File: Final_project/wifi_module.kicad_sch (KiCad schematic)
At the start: 3 parts, among them U4 ESP32-WROOM-32

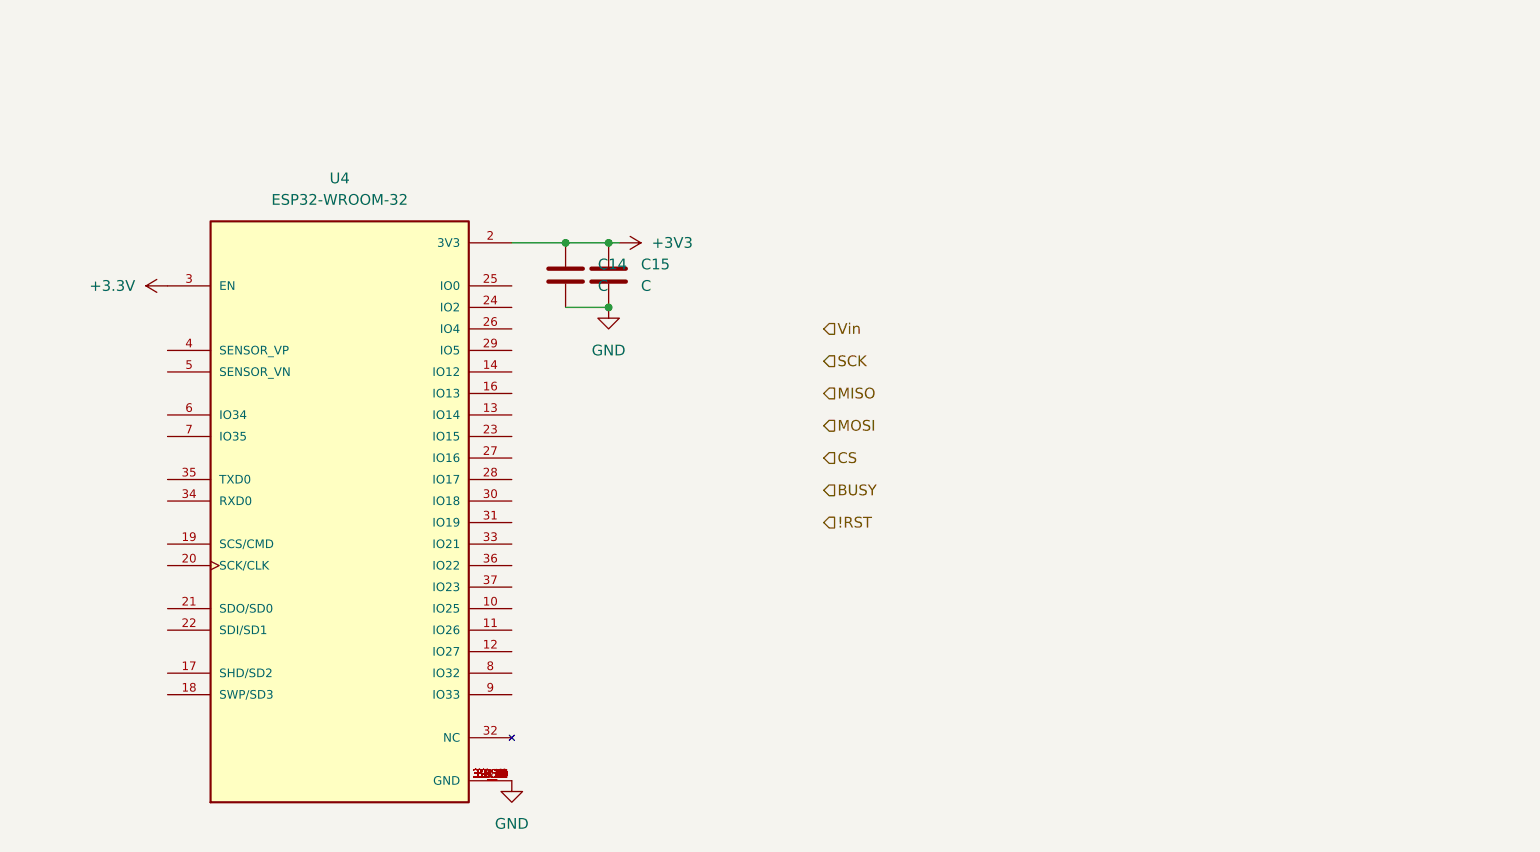
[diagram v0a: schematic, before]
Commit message: Complete wifi module airlift
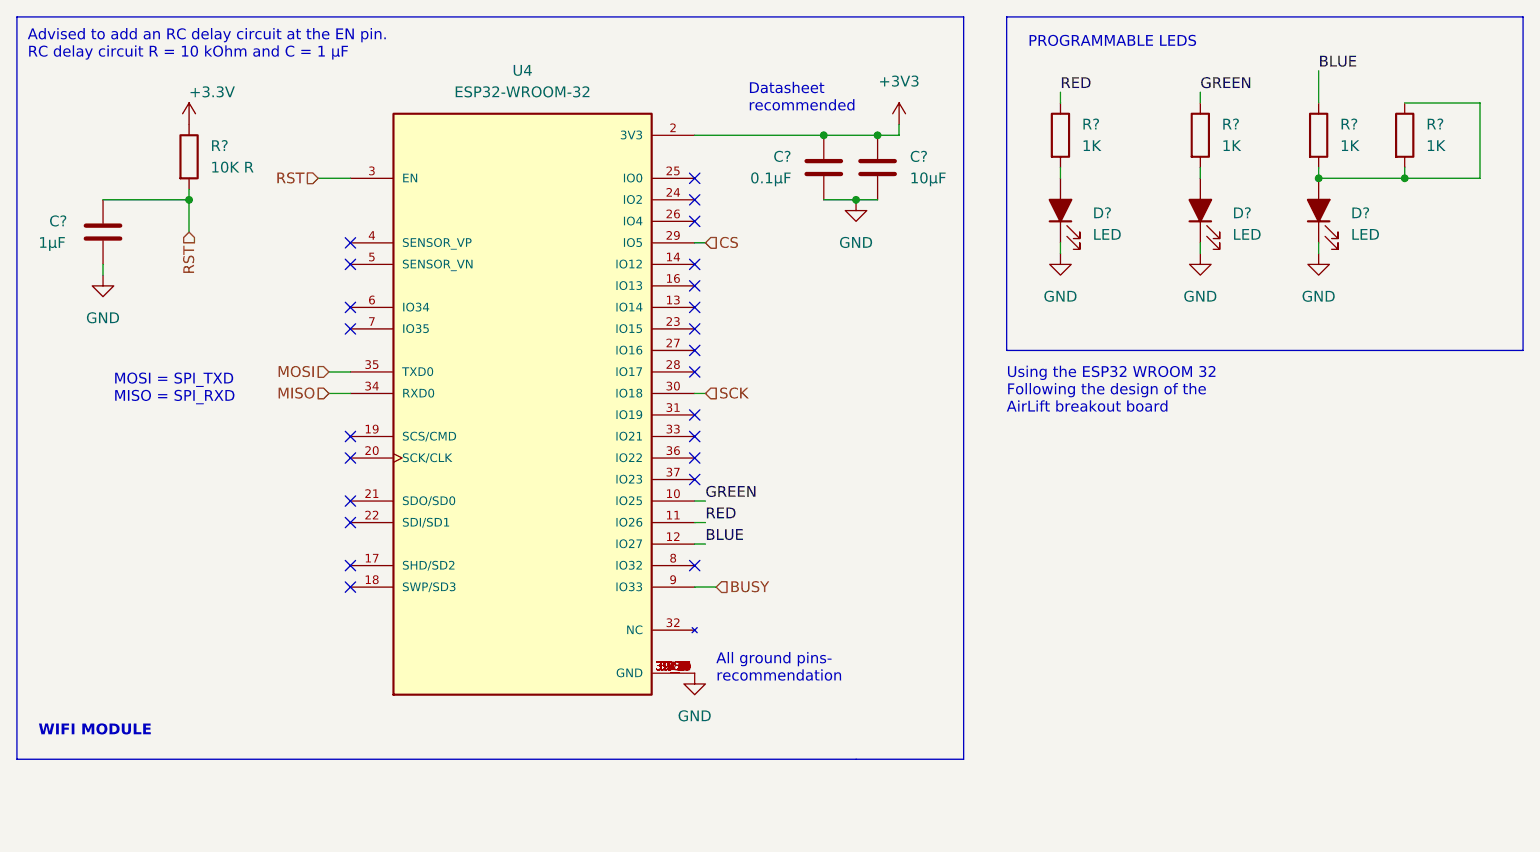
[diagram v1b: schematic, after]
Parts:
- removed C14, C15: C, Capacitor_SMD:C_0603_1608Metric, symbol Device:C
- added C?: 10µF, Final_project:GRM188R61E106KA73D, symbol Device:C
- added C?: 0.1µF, Final_project:CL10B104JB8NNNC, symbol Device:C
- added C?: 1µF, Final_project:CL10B105KA8NNNC, symbol Device:C
- added D? (x3): LED, Final_project:LTST-C170TBKT, symbol Device:LED_Filled
- added R? (x4): 1K, Final_project:RC0603FR-071KL, symbol Device:R
- added R?: 10K R, Resistor_SMD:R_0805_2012Metric, symbol Device:R
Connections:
- net +3.3V: now also R?.1; no longer U4.3 (EN)
- net +3V3: now also C?.1, C?.1
- net BUSY: now also U4.9 (IO33)
- net CS: now also U4.29 (IO5)
- net GND: now also C?.1, C?.2, C?.2, D?.1 (K), D?.1 (K), D?.1 (K)
- net MISO: now also U4.34 (RXD0)
- net MOSI: now also U4.35 (TXD0)
- net SCK: now also U4.30 (IO18)
- net GREEN: now reaches U4.10 (IO25)
- net GREEN: now also R?.1
- net RED: now reaches U4.11 (IO26)
- net RED: now also R?.1
- net BLUE: now reaches U4.12 (IO27)
- net BLUE: now also R?.1
- new net: D?.2 (A), R?.1, R?.2, R?.2
- new net: D?.2 (A), R?.2 (x2)
- new net RST: C?.2, R?.2, U4.3 (EN)
- no-connect marks 0 -> 24
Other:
- note added: "Advised to add an RC delay circuit at the EN pin. RC delay circuit R = 10 kOhm and C = 1 μF"
- note added: "All ground pins- recommendation"
- note added: "Datasheet recommended"
- note added: "MOSI = SPI_TXD MISO = SPI_RXD"
- note added: "PROGRAMMABLE LEDS"
- note added: "Using the ESP32 WROOM 32 Following the design of the AirLift breakout board"
- note added: "WIFI MODULE"
- moved on the sheet: U4

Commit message: Add light sensing sheet
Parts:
- gave numbers to parts that had none: 11
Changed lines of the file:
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@@
   (symbol (lib_id "power:+3.3V") (at 35.56 26.67 0) (unit 1)
     (in_bom yes) (on_board yes)
-    (property "Reference" "#PWR?" (id 0) (at 35.56 30.48 0)
+    (property "Reference" "#PWR0136" (id 0) (at 35.56 30.48 0)
       (effects (font (size 1.27 1.27)) hide)
     )
@@
   (symbol (lib_id "Device:R") (at 168.91 27.94 0) (unit 1)
     (in_bom yes) (on_board yes) (fields_autoplaced)
-    (property "Reference" "R?" (id 0) (at 171.45 26.6699 0)
+    (property "Reference" "R12" (id 0) (at 171.45 26.6699 0)
       (effects (font (size 1.27 1.27)) (justify left))
     )
@@
   (symbol (lib_id "Device:C") (at 116.84 31.75 0) (unit 1)
     (in_bom yes) (on_board yes) (fields_autoplaced)
-    (property "Reference" "C?" (id 0) (at 120.65 30.4799 0)
+    (property "Reference" "C16" (id 0) (at 120.65 30.4799 0)
       (effects (font (size 1.27 1.27)) (justify left))
     )
@@
   (symbol (lib_id "Device:R") (at 154.94 27.94 0) (unit 1)
     (in_bom yes) (on_board yes) (fields_autoplaced)
-    (property "Reference" "R?" (id 0) (at 157.48 26.6699 0)
+    (property "Reference" "R11" (id 0) (at 157.48 26.6699 0)
       (effects (font (size 1.27 1.27)) (justify left))
     )
@@
   (symbol (lib_id "Device:LED_Filled") (at 154.94 36.83 90) (unit 1)
     (in_bom yes) (on_board yes) (fields_autoplaced)
-    (property "Reference" "D?" (id 0) (at 158.75 37.1474 90)
+    (property "Reference" "D4" (id 0) (at 158.75 37.1474 90)
       (effects (font (size 1.27 1.27)) (justify right))
     )
@@
   (symbol (lib_id "Device:LED_Filled") (at 168.91 36.83 90) (unit 1)
     (in_bom yes) (on_board yes) (fields_autoplaced)
-    (property "Reference" "D?" (id 0) (at 172.72 37.1474 90)
+    (property "Reference" "D5" (id 0) (at 172.72 37.1474 90)
       (effects (font (size 1.27 1.27)) (justify right))
     )
@@
   (symbol (lib_id "Device:R") (at 138.43 27.94 0) (unit 1)
     (in_bom yes) (on_board yes) (fields_autoplaced)
-    (property "Reference" "R?" (id 0) (at 140.97 26.6699 0)
+    (property "Reference" "R10" (id 0) (at 140.97 26.6699 0)
       (effects (font (size 1.27 1.27)) (justify left))
     )
@@
   (symbol (lib_id "power:GND") (at 138.43 41.91 0) (unit 1)
     (in_bom yes) (on_board yes) (fields_autoplaced)
-    (property "Reference" "#PWR?" (id 0) (at 138.43 48.26 0)
+    (property "Reference" "#PWR0128" (id 0) (at 138.43 48.26 0)
       (effects (font (size 1.27 1.27)) hide)
     )
@@
   (symbol (lib_id "power:GND") (at 168.91 41.91 0) (unit 1)
     (in_bom yes) (on_board yes) (fields_autoplaced)
-    (property "Reference" "#PWR?" (id 0) (at 168.91 48.26 0)
+    (property "Reference" "#PWR0134" (id 0) (at 168.91 48.26 0)
       (effects (font (size 1.27 1.27)) hide)
     )
@@
   (symbol (lib_id "power:GND") (at 154.94 41.91 0) (unit 1)
     (in_bom yes) (on_board yes) (fields_autoplaced)
-    (property "Reference" "#PWR?" (id 0) (at 154.94 48.26 0)
+    (property "Reference" "#PWR0133" (id 0) (at 154.94 48.26 0)
       (effects (font (size 1.27 1.27)) hide)
     )
@@
   (symbol (lib_id "Device:C") (at 110.49 31.75 0) (unit 1)
     (in_bom yes) (on_board yes)
-    (property "Reference" "C?" (id 0) (at 106.68 30.48 0)
+    (property "Reference" "C15" (id 0) (at 106.68 30.48 0)
       (effects (font (size 1.27 1.27)) (justify right))
     )
@@
   (symbol (lib_id "Device:LED_Filled") (at 138.43 36.83 90) (unit 1)
     (in_bom yes) (on_board yes) (fields_autoplaced)
-    (property "Reference" "D?" (id 0) (at 142.24 37.1474 90)
+    (property "Reference" "D3" (id 0) (at 142.24 37.1474 90)
       (effects (font (size 1.27 1.27)) (justify right))
     )
@@
   (symbol (lib_id "Device:R") (at 35.56 30.48 0) (unit 1)
     (in_bom yes) (on_board yes) (fields_autoplaced)
-    (property "Reference" "R?" (id 0) (at 38.1 29.2099 0)
+    (property "Reference" "R9" (id 0) (at 38.1 29.2099 0)
       (effects (font (size 1.27 1.27)) (justify left))
     )
@@
   (symbol (lib_id "Device:R") (at 179.07 27.94 0) (unit 1)
     (in_bom yes) (on_board yes) (fields_autoplaced)
-    (property "Reference" "R?" (id 0) (at 181.61 26.6699 0)
+    (property "Reference" "R13" (id 0) (at 181.61 26.6699 0)
       (effects (font (size 1.27 1.27)) (justify left))
     )
@@
   (symbol (lib_id "Device:C") (at 25.4 39.37 180) (unit 1)
     (in_bom yes) (on_board yes)
-    (property "Reference" "C?" (id 0) (at 19.05 38.1 0)
+    (property "Reference" "C14" (id 0) (at 19.05 38.1 0)
       (effects (font (size 1.27 1.27)) (justify right))
     )
@@
   (symbol (lib_id "power:GND") (at 25.4 44.45 0) (unit 1)
     (in_bom yes) (on_board yes) (fields_autoplaced)
-    (property "Reference" "#PWR?" (id 0) (at 25.4 50.8 0)
-      (effects (font (size 1.27 1.27)) hide)
-    )
+    (property "Reference" "#PWR0135" (id 0) (at 25.4 50.8 0)
+      (effects (font (size 1.27 1.27)) hide)
+    )

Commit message: Add 3d, fixing vias and layout issues
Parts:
- C14: footprint Final_project:CL10B105KA8NNNC -> Capacitor_SMD:C_0603_1608Metric; Digi-Key_Part (none) -> CL10B105KA8NNNC
- C15: footprint Final_project:CL10B104JB8NNNC -> Capacitor_SMD:C_0603_1608Metric; Digi-Key_Part (none) -> CL10B105KA8NNNC
- C16: footprint Final_project:GRM188R61E106KA73D -> Capacitor_SMD:C_0603_1608Metric; Digi-Key_Part (none) -> GRM188R61E106KA73D
- R10, R11, R12: footprint Final_project:RC0603FR-071KL -> Resistor_SMD:R_0603_1608Metric; Digi-Key_Part (none) -> RC0603FR-071KL
- R13: footprint Final_project:RC0603FR-071KL -> Resistor_SMD:R_0603_1608Metric
- R9: value 10K R -> 10K
- U4: footprint Final_project:MODULE_ESP32-WROOM-32 -> MODULE_ESP32-WROOM-32
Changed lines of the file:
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@@
     (property "Reference" "U4" (id 0) (at 74.93 20.32 0))
     (property "Value" "ESP32-WROOM-32" (id 1) (at 74.93 22.86 0))
-    (property "Footprint" "Final_project:MODULE_ESP32-WROOM-32" (id 2) (at 74.93 60.96 0)
+    (property "Footprint" "MODULE_ESP32-WROOM-32" (id 2) (at 74.93 60.96 0)
       (effects (font (size 1.27 1.27)) (justify left bottom) hide)
     )
@@
       (effects (font (size 1.27 1.27)) (justify left))
     )
-    (property "Footprint" "Final_project:RC0603FR-071KL" (id 2) (at 167.132 27.94 90)
+    (property "Footprint" "Resistor_SMD:R_0603_1608Metric" (id 2) (at 167.132 27.94 90)
       (effects (font (size 1.27 1.27)) hide)
     )
@@
       (effects (font (size 1.27 1.27)) hide)
     )
+    (property "Digi-Key_Part" "RC0603FR-071KL" (id 4) (at 168.91 27.94 0)
+      (effects (font (size 1.27 1.27)) hide)
+    )
     (pin "1")
     (pin "2")
@@
       (effects (font (size 1.27 1.27)) (justify left))
     )
-    (property "Footprint" "Final_project:GRM188R61E106KA73D" (id 2) (at 117.8052 35.56 0)
-      (effects (font (size 1.27 1.27)) hide)
-    )
-    (property "Datasheet" "~" (id 3) (at 116.84 31.75 0)
+    (property "Footprint" "Capacitor_SMD:C_0603_1608Metric" (id 2) (at 117.8052 35.56 0)
+      (effects (font (size 1.27 1.27)) hide)
+    )
+    (property "Datasheet" "https://search.murata.co.jp/Ceramy/image/img/A01X/G101/ENG/GRM188R61E106KA73-01.pdf" (id 3) (at 116.84 31.75 0)
+      (effects (font (size 1.27 1.27)) hide)
+    )
+    (property "Digi-Key_Part" "GRM188R61E106KA73D" (id 4) (at 116.84 31.75 0)
       (effects (font (size 1.27 1.27)) hide)
     )
@@
       (effects (font (size 1.27 1.27)) (justify left))
     )
-    (property "Footprint" "Final_project:RC0603FR-071KL" (id 2) (at 153.162 27.94 90)
-      (effects (font (size 1.27 1.27)) hide)
-    )
-    (property "Datasheet" "~" (id 3) (at 154.94 27.94 0)
+    (property "Footprint" "Resistor_SMD:R_0603_1608Metric" (id 2) (at 153.162 27.94 90)
+      (effects (font (size 1.27 1.27)) hide)
+    )
+    (property "Datasheet" "https://www.yageo.com/upload/media/product/productsearch/datasheet/rchip/PYu-RC_Group_51_RoHS_L_12.pdf" (id 3) (at 154.94 27.94 0)
+      (effects (font (size 1.27 1.27)) hide)
+    )
+    (property "Digi-Key_Part" "RC0603FR-071KL" (id 4) (at 154.94 27.94 0)
       (effects (font (size 1.27 1.27)) hide)
     )
@@
       (effects (font (size 1.27 1.27)) (justify left))
     )
-    (property "Footprint" "Final_project:RC0603FR-071KL" (id 2) (at 136.652 27.94 90)
-      (effects (font (size 1.27 1.27)) hide)
-    )
-    (property "Datasheet" "~" (id 3) (at 138.43 27.94 0)
+    (property "Footprint" "Resistor_SMD:R_0603_1608Metric" (id 2) (at 136.652 27.94 90)
+      (effects (font (size 1.27 1.27)) hide)
+    )
+    (property "Datasheet" "https://www.yageo.com/upload/media/product/productsearch/datasheet/rchip/PYu-RC_Group_51_RoHS_L_12.pdf" (id 3) (at 138.43 27.94 0)
+      (effects (font (size 1.27 1.27)) hide)
+    )
+    (property "Digi-Key_Part" "RC0603FR-071KL" (id 4) (at 138.43 27.94 0)
       (effects (font (size 1.27 1.27)) hide)
     )
@@
       (effects (font (size 1.27 1.27)) (justify right))
     )
-    (property "Footprint" "Final_project:CL10B104JB8NNNC" (id 2) (at 111.4552 35.56 0)
+    (property "Footprint" "Capacitor_SMD:C_0603_1608Metric" (id 2) (at 111.4552 35.56 0)
       (effects (font (size 1.27 1.27)) hide)
     )
@@
       (effects (font (size 1.27 1.27)) hide)
     )
+    (property "Digi-Key_Part" "CL10B105KA8NNNC" (id 4) (at 110.49 31.75 0)
+      (effects (font (size 1.27 1.27)) hide)
+    )
     (pin "1")
     (pin "2")
@@
       (effects (font (size 1.27 1.27)) (justify left))
     )
-    (property "Value" "10K R" (id 1) (at 38.1 31.7499 0)
+    (property "Value" "10K" (id 1) (at 38.1 31.7499 0)
       (effects (font (size 1.27 1.27)) (justify left))
     )
@@
       (effects (font (size 1.27 1.27)) hide)
     )
-    (property "Datasheet" "https://www.yageo.com/upload/media/product/productsearch/datasheet/rchip/PYu-RC_Group_51_RoHS_L_12.pdf" (id 3) (at 35.56 30.48 0)
+    (property "Datasheet" "~" (id 3) (at 35.56 30.48 0)
       (effects (font (size 1.27 1.27)) hide)
     )
@@
       (effects (font (size 1.27 1.27)) (justify left))
     )
-    (property "Footprint" "Final_project:RC0603FR-071KL" (id 2) (at 177.292 27.94 90)
+    (property "Footprint" "Resistor_SMD:R_0603_1608Metric" (id 2) (at 177.292 27.94 90)
       (effects (font (size 1.27 1.27)) hide)
     )
@@
       (effects (font (size 1.27 1.27)) (justify right))
     )
-    (property "Footprint" "Final_project:CL10B105KA8NNNC" (id 2) (at 24.4348 35.56 0)
+    (property "Footprint" "Capacitor_SMD:C_0603_1608Metric" (id 2) (at 24.4348 35.56 0)
       (effects (font (size 1.27 1.27)) hide)
     )
@@
       (effects (font (size 1.27 1.27)) hide)
     )
+    (property "Digi-Key_Part" "CL10B105KA8NNNC" (id 4) (at 25.4 39.37 0)
+      (effects (font (size 1.27 1.27)) hide)
+    )
